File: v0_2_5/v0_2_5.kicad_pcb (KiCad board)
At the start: 2 copper layers, 91.4 x 50.8 mm, 59 parts, among them IC1 RASPBERRY_PI_PICO_W, IC2 BH1750FVI-TR, IC3 AP2138N-3.3TRG1, J1 S2B-PH-SM4-TB_LF__SN_, J2 HYCW110-TF10-180B, J4 SM04B-SRSS-TB, J5 Screw_Terminal_01x03, J6 Conn_01x02_Pin, Q1 DMG2301L-7, Q2 DMG2301L-7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

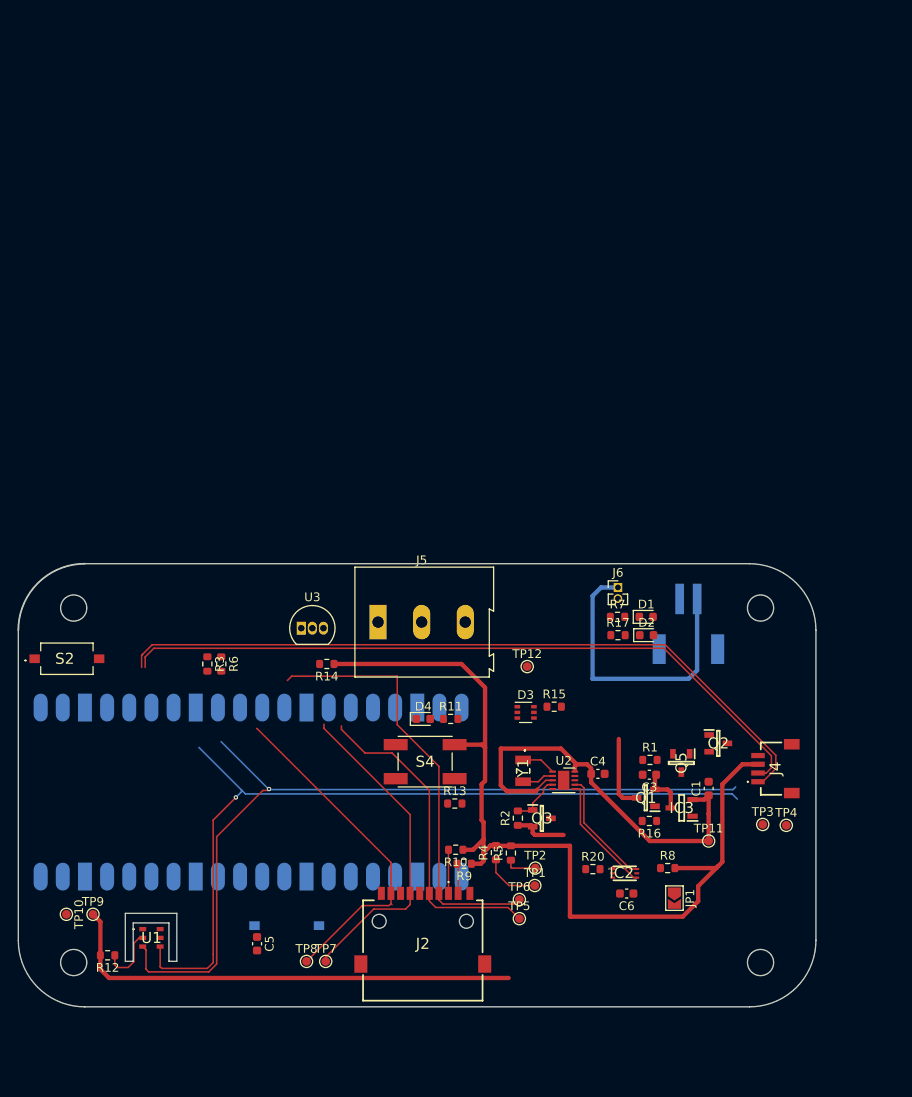
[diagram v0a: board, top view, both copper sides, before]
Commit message: new replacement v2.5
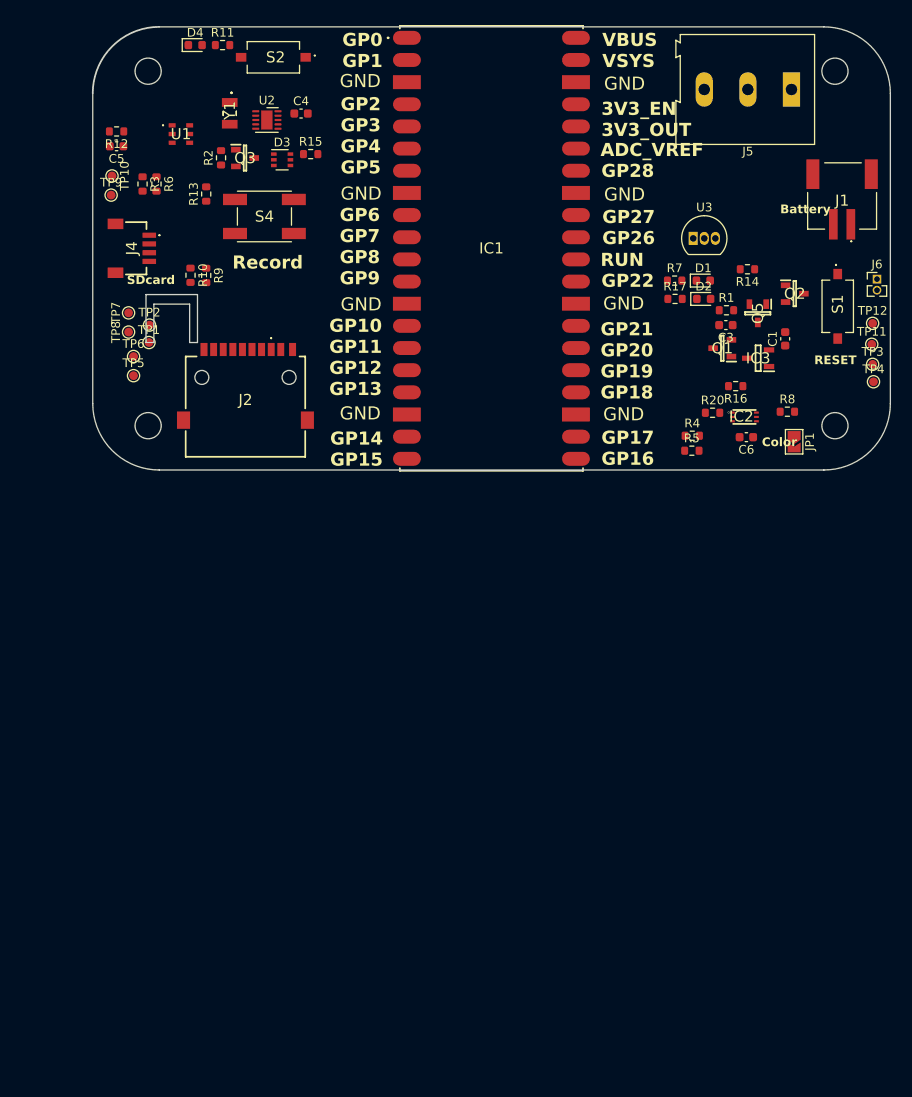
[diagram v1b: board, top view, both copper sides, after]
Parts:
- IC1, J1, S1: moved to F.Cu
- moved J4 95.3 mm to (111.8, 27.6), turned to -90 degrees
- moved S1 95.0 mm to (193.0, 34.3), turned to -90 degrees
- moved R12 94.5 mm to (110.4, 14.2)
- moved C5 92.8 mm to (110.4, 15.9), turned to 180 degrees
- moved U1 92.2 mm to (117.7, 14.6)
- moved TP10 84.8 mm to (109.8, 19.4)
- moved Q3 83.0 mm to (125.1, 17.3)
- moved U2 83.0 mm to (127.6, 12.9)
- moved C4 83.0 mm to (131.5, 12.2)
- moved R2 83.0 mm to (122.3, 17.3)
- moved Y1 82.5 mm to (123.3, 12.2)
- moved TP9 82.5 mm to (109.7, 21.6)
- moved D4 81.6 mm to (119.4, 4.35)
- moved R11 81.6 mm to (122.5, 4.35)
- moved TP7 77.7 mm to (111.7, 35.0), turned to 90 degrees
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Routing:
- net /I2C1_SCL: track 193.1 -> 0.00 mm, vias 1 -> 0
- net /I2C1_SDA: track 189.4 -> 0.00 mm, vias 1 -> 0
- net +3.3V: track 159.0 -> 0.00 mm
- net V+_A0: track 54.7 -> 0.00 mm
- net /CS: track 50.1 -> 0.00 mm
- net +BATT: track 41.9 -> 0.00 mm
- net /MISO: track 39.1 -> 0.00 mm
- net /SCK: track 37.4 -> 0.00 mm
- net /MOSI: track 37.2 -> 0.00 mm
- net Net-(U1-VDD): track 7.09 -> 0.00 mm
- net /I2C0_SCL: track 6.53 -> 0.00 mm
- net Net-(U2-~{INT}): track 5.93 -> 0.00 mm
- net /LDO/VIN: track 5.45 -> 0.00 mm
- net /SDcard/DAT2: track 5.00 -> 0.00 mm
- net Net-(U2-OSCI): track 3.94 -> 0.00 mm
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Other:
- outline, holes or cut-outs redrawn
- board text added: "3V3_EN 3V3_OUT"
- board text added: "ADC_VREF"
- board text added: "Battery"
- board text added: "Color"
- board text added: "GND"
- board text added: "GP0 GP1"
- board text added: "GP10 GP11 GP12 GP13"
- board text added: "GP14 GP15"
- board text added: "GP17 GP16"
- board text added: "GP2 GP3 GP4 GP5"
- board text added: "GP21 GP20 GP19 GP18"
- board text added: "GP22"
- board text added: "GP27 GP26"
- board text added: "GP28"
- board text added: "GP6 GP7 GP8 GP9"
- board text added: "RUN"
- board text added: "Record"
- board text added: "SDcard"
- board text added: "VBUS VSYS"

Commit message: add label
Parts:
- moved J5 38.3 mm to (175.8, 45.9), turned to 0 degrees
- moved U3 22.0 mm to (191.1, 43.0)
- moved J6 20.1 mm to (192.6, 11.7)
- moved J1 16.2 mm to (184.8, 8.05)
- moved R4 14.6 mm to (175.2, 34.5)
- moved R5 14.6 mm to (175.2, 36.3)
- moved JP1 13.5 mm to (187.8, 36.4)
- moved C6 13.0 mm to (182.3, 36.4)
- moved IC2 13.0 mm to (182.1, 34.0)
- moved R8 12.5 mm to (188.0, 33.9)
- moved R20 12.2 mm to (178.5, 34.4)
- moved R16 11.3 mm to (180.9, 32.1)
- moved C3 11.0 mm to (180.8, 25.5)
- moved D1 11.0 mm to (178.2, 20.4)
- moved D2 11.0 mm to (178.3, 22.5)
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
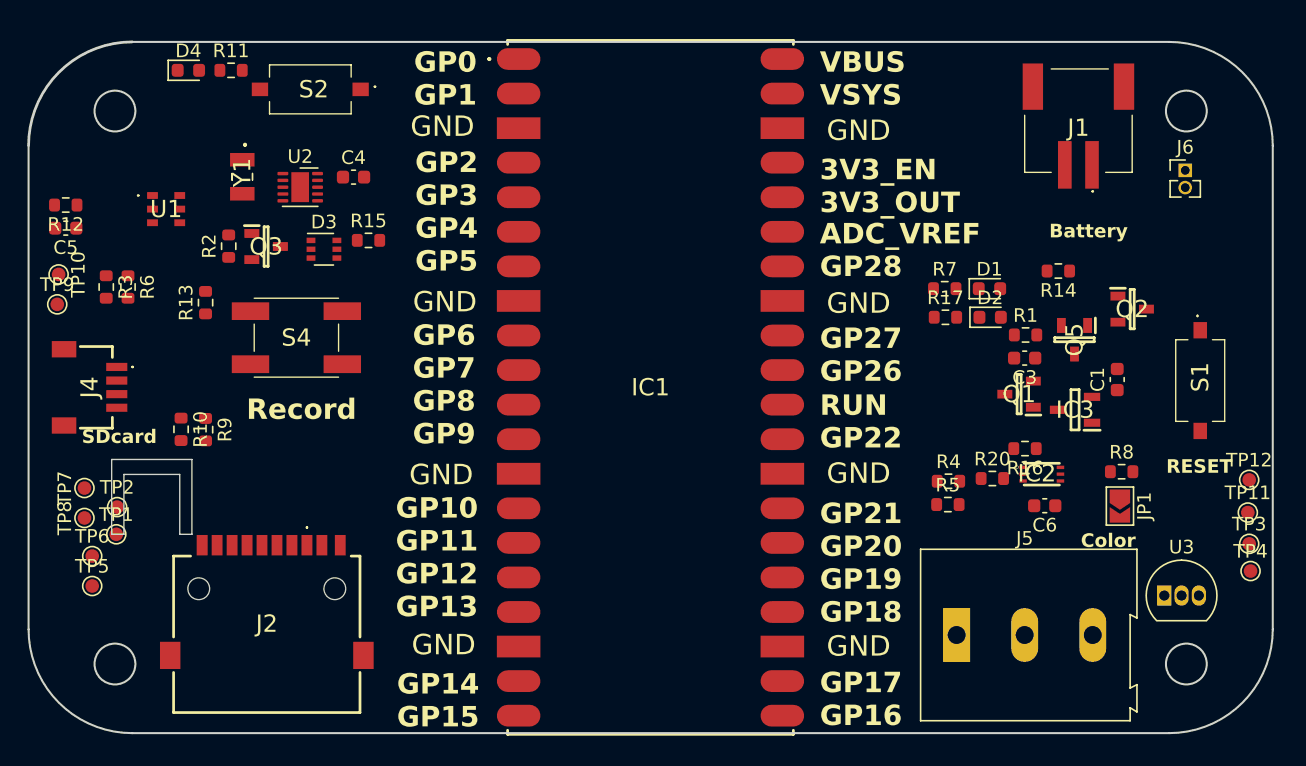
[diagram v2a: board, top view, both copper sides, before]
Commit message: route almost done:
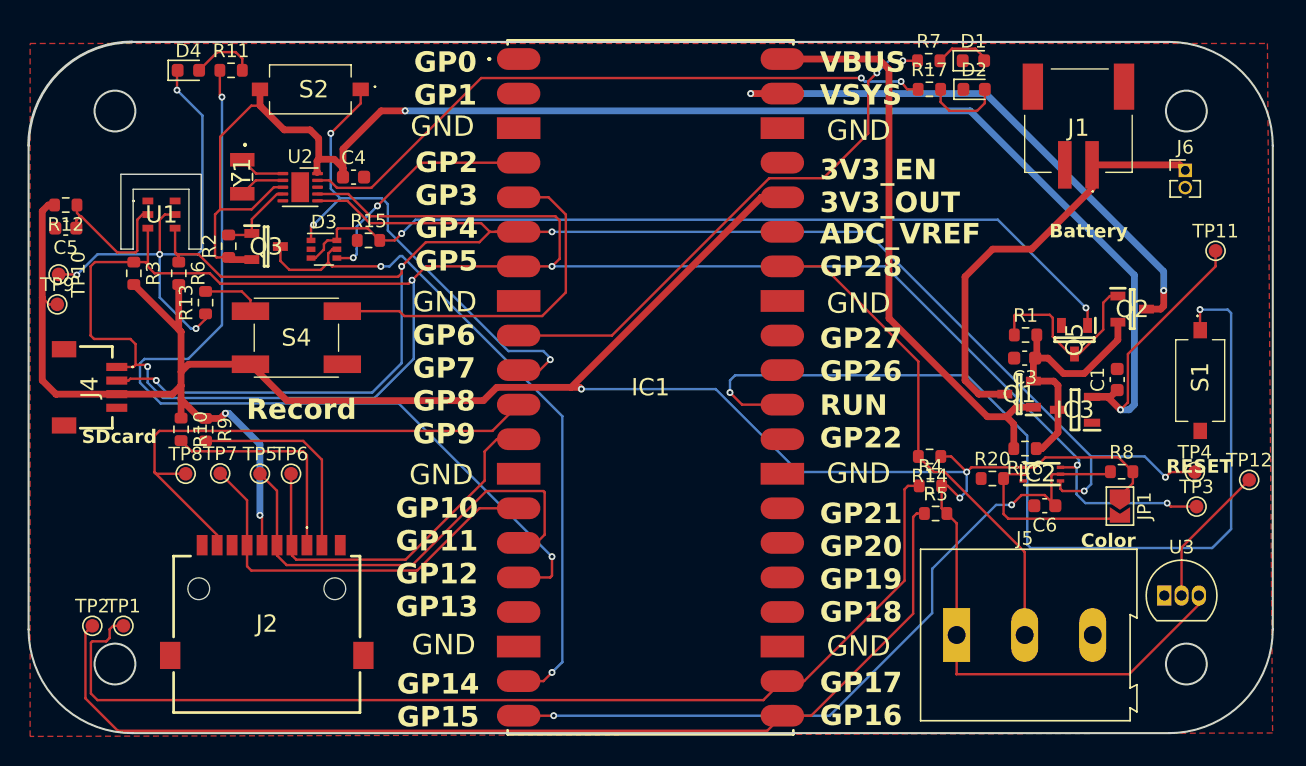
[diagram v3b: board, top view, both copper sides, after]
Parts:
- moved TP11 19.4 mm to (194.9, 17.6)
- moved R7 16.8 mm to (173.8, 3.65)
- moved D1 16.8 mm to (177.1, 3.65)
- moved D2 16.8 mm to (177.1, 5.75)
- moved R17 16.8 mm to (173.8, 5.75)
- moved R14 16.6 mm to (173.8, 32.7)
- moved TP6 15.8 mm to (126.9, 34.0)
- moved TP5 14.8 mm to (124.6, 34.0)
- moved TP7 10.0 mm to (121.7, 34.0), turned to 0 degrees
- moved TP2 8.91 mm to (112.3, 45.2)
- moved TP4 8.35 mm to (193.3, 33.9)
- moved TP8 8.12 mm to (119.2, 34.0), turned to 0 degrees
- moved TP1 6.75 mm to (114.6, 45.2)
- moved TP3 4.74 mm to (193.5, 36.4)
- moved R6 3.86 mm to (118.7, 19.3)
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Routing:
- net +3.3V: track 0.00 -> 195.2 mm, vias 0 -> 5
- net /I2C1_SCL: track 0.00 -> 158.8 mm, vias 0 -> 5
- net /I2C1_SDA: track 0.00 -> 137.6 mm, vias 0 -> 5
- net V+_A0: track 0.00 -> 128.9 mm, vias 0 -> 2
- net /I2C0_SDA: track 0.00 -> 79.0 mm
- net /I2C0_SCL: track 0.00 -> 78.5 mm
- net /RUN: track 0.00 -> 72.4 mm, vias 0 -> 2
- net /Record: track 0.00 -> 66.9 mm, vias 0 -> 2
- net /VSYS_EN: track 0.00 -> 63.6 mm, vias 0 -> 2
- net /RESET: track 0.00 -> 55.2 mm, vias 0 -> 2
- net /RTC_ALARM: track 0.00 -> 51.2 mm, vias 0 -> 2
- net /ALARM_LED: track 0.00 -> 48.2 mm, vias 0 -> 2
- net /DQ: track 0.00 -> 47.3 mm
- net VBUS: track 0.00 -> 42.9 mm
- net VSYS: track 0.00 -> 42.0 mm, vias 0 -> 2
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- added copper zone on F.Cu, net GND
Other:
- outline, holes or cut-outs redrawn

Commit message: replacement
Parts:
- removed U3: DS18B20, Package_TO_SOT_THT:TO-92_Inline
- moved C5 20.5 mm to (129.6, 23.1), turned to 0 degrees
- moved R3 16.2 mm to (130.7, 24.7), turned to 0 degrees
- moved R12 14.6 mm to (120.8, 24.5)
- moved TP9 13.7 mm to (111.0, 35.1)
- moved R6 12.1 mm to (130.6, 21.4), turned to 0 degrees
- moved U1 11.5 mm to (125.5, 23.1), turned to 90 degrees
- moved JP1 9.64 mm to (178.2, 35.7)
- moved S4 7.94 mm to (128.6, 31.8)
- moved R8 7.00 mm to (181.1, 32.2), turned to 180 degrees
- moved R13 6.31 mm to (123.5, 27.0), turned to 0 degrees
- moved TP6 5.22 mm to (121.7, 33.6)
- moved TP5 4.78 mm to (119.9, 34.9)
- moved C4 4.59 mm to (127.5, 9.87), turned to 90 degrees
- moved R15 4.26 mm to (128.6, 15.3)
- moved R20 3.72 mm to (181.0, 37.0), turned to -90 degrees
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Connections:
- IC1 pad 13: unconnected-(IC1-GND_3-Pad13) -> GND
- IC1 pad 18: unconnected-(IC1-GND_4-Pad18) -> GND
- IC1 pad 23: unconnected-(IC1-GND_5-Pad23) -> GND
- IC1 pad 28: unconnected-(IC1-GND_6-Pad28) -> GND
- IC1 pad 3: unconnected-(IC1-GND_1-Pad3) -> GND
- IC1 pad 38: unconnected-(IC1-GND_7-Pad38) -> GND
- IC1 pad 8: unconnected-(IC1-GND_2-Pad8) -> GND
- J4 pad 1: /I2C1_SCL -> /I2C0_SCL
- J4 pad 2: /I2C1_SDA -> /I2C0_SDA
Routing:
- net /RESET: track 55.2 -> 114.7 mm
- net /I2C1_SCL: track 158.8 -> 106.4 mm, vias 5 -> 3
- net +3.3V: track 195.2 -> 147.3 mm, vias 5 -> 8
- net /I2C1_SDA: track 137.6 -> 97.4 mm, vias 5 -> 3
- net /I2C0_SDA: track 79.0 -> 99.8 mm
- net /I2C0_SCL: track 78.5 -> 99.4 mm
- net GND: track 37.3 -> 54.1 mm, vias 4 -> 6
- net /Record: track 66.9 -> 79.0 mm
- net /DQ: track 47.3 -> 55.3 mm
- net V+_A0: track 128.9 -> 121.6 mm
- net Net-(U1-VDD): track 10.5 -> 3.93 mm
- net Net-(IC2-ADDR): track 12.9 -> 7.36 mm
- net /CS: track 27.7 -> 32.1 mm
- net /RTC_ALARM: track 51.2 -> 55.5 mm
- net Net-(D2-A): track 5.70 -> 1.68 mm
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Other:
- outline, holes or cut-outs redrawn
- board text added: "+"
- board text added: "-"
- board text added: "3.3V"
- board text added: "CS"
- board text added: "MISO"
- board text added: "MOSI"
- board text added: "SCK"
- board text added: "STATUS"
- board text added: "V+"

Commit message: change placement
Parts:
- moved TP9 88.3 mm to (197.0, 15.1)
- moved TP10 87.4 mm to (197.0, 12.9)
- moved J4 83.5 mm to (195.3, 27.6), turned to 90 degrees
- moved TP2 82.0 mm to (191.8, 40.1)
- moved TP1 79.5 mm to (194.4, 40.6)
- moved J5 62.7 mm to (114.5, 33.2), turned to 90 degrees
- moved R14 61.4 mm to (115.2, 14.6)
- moved U2 58.8 mm to (183.1, 32.2)
- moved C4 58.8 mm to (183.0, 29.2)
- moved R2 58.6 mm to (178.2, 34.7), turned to 0 degrees
- moved Y1 58.5 mm to (178.7, 31.1)
- moved R15 57.6 mm to (182.9, 34.6)
- moved R5 27.2 mm to (197.1, 22.2)
- moved S1 24.1 mm to (184.7, 49.5), turned to 0 degrees
- moved R4 21.6 mm to (195.5, 33.7)
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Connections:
- IC1 pad 16: /Record -> unconnected-(IC1-UART0_TX/I2C0_SDA_/SPI1_RX_/GP12-Pad16)
- IC1 pad 17: unconnected-(IC1-UART0_RX/I2C0_SCL_/SPI1_CSN/GP13-Pad17) -> /Record
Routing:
- net /RUN: track 72.4 -> 0.00 mm, vias 2 -> 0
- net /RESET: track 114.7 -> 48.7 mm
- net /VSYS_EN: track 64.8 -> 0.00 mm, vias 2 -> 0
- net +3.3V: track 147.3 -> 205.4 mm
- net /DQ: track 55.3 -> 0.00 mm
- net /ALARM_LED: track 49.0 -> 0.00 mm, vias 2 -> 0
- net GND: track 54.1 -> 9.79 mm, vias 6 -> 2
- net /I2C0_SCL: track 99.4 -> 56.7 mm
- net /I2C0_SDA: track 99.8 -> 58.2 mm
- net /ACT_LED: track 39.9 -> 0.00 mm, vias 2 -> 0
- net /SWITCH_STATUS: track 39.5 -> 0.00 mm, vias 3 -> 0
- net /RTC_ALARM: track 55.5 -> 91.8 mm, vias 2 -> 1
- net /Button: track 29.5 -> 0.00 mm
- net /HOLD_VSYS_EN: track 17.7 -> 0.00 mm, vias 2 -> 0
- net /MOSI: track 37.0 -> 19.6 mm
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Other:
- outline, holes or cut-outs redrawn
- board text added: "DQ"
- board text added: "HOLD BUTTON I2C-SDA I2C-SCL"
- board text added: "I2C"
- board text added: "I2C0-SCL I2C0-SDA"
- board text added: "LED STATUS MISO CS"
- board text added: "Power"
- board text added: "RTC_AL RESET"
- board text added: "Real Time"
- board text added: "Reset"
- board text added: "SCK MOSI"
- board text added: "Status"
- board text added: "Temperature Humidity"
- board text removed: "ADC_VREF"
- board text removed: "Battery"
- board text removed: "GP0 GP1"
- board text removed: "GP10 GP11 GP12 GP13"
- board text removed: "GP14 GP15"
- board text removed: "GP17 GP16"
- board text removed: "GP2 GP3 GP4 GP5"
- board text removed: "GP21 GP20 GP19 GP18"
- board text removed: "GP22"
- board text removed: "GP27 GP26"
- board text removed: "GP28"
- board text removed: "GP6 GP7 GP8 GP9"
- board text removed: "RESET"
- board text removed: "STATUS"

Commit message: done
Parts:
- moved TP11 84.9 mm to (111.5, 14.9)
- moved TP4 80.1 mm to (118.8, 15.3)
- moved TP12 79.6 mm to (113.3, 17.4)
- moved TP3 76.7 mm to (118.8, 17.7)
- moved TP9 28.2 mm to (188.5, 42.0)
- moved TP6 20.4 mm to (134.2, 31.3)
- moved R5 13.2 mm to (192.0, 34.4)
- moved R12 11.5 mm to (129.8, 18.8), turned to -90 degrees
- moved TP5 5.86 mm to (112.7, 44.7)
- moved R8 5.78 mm to (186.2, 40.1), turned to 0 degrees
- moved TP10 3.10 mm to (195.2, 15.5)
- moved TP2 2.92 mm to (191.9, 37.2)
- moved TP7 2.84 mm to (112.7, 41.7)
- moved TP1 2.57 mm to (191.9, 39.7)
- moved TP8 1.82 mm to (112.7, 39.1)
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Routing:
- net /VSYS_EN: track 0.00 -> 102.8 mm, vias 0 -> 4
- net Net-(U2-~{INT}): track 0.00 -> 83.7 mm, vias 0 -> 2
- net /DQ: track 0.00 -> 72.2 mm, vias 0 -> 1
- net /ALARM_LED: track 0.00 -> 61.5 mm, vias 0 -> 2
- net /SWITCH_STATUS: track 0.00 -> 56.1 mm, vias 0 -> 2
- net /RUN: track 0.00 -> 44.5 mm, vias 0 -> 2
- net /ACT_LED: track 0.00 -> 43.3 mm, vias 0 -> 2
- net V+_A0: track 117.8 -> 147.9 mm
- net /Button: track 0.00 -> 26.2 mm, vias 0 -> 2
- net +3.3V: track 205.4 -> 231.0 mm, vias 8 -> 9
- net /HOLD_VSYS_EN: track 0.00 -> 23.9 mm, vias 0 -> 2
- net /RESET: track 48.7 -> 66.4 mm
- net /SCK: track 31.2 -> 48.9 mm
- net /MOSI: track 19.6 -> 36.7 mm, vias 0 -> 2
- net Net-(Q2-Pad1): track 0.00 -> 16.6 mm, vias 0 -> 2
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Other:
- board text added: "RESET"
- board text added: "RTC_AL"
- board text removed: "RTC_AL RESET"
